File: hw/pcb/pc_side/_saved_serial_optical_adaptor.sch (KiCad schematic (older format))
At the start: 13 parts, among them P1 USB_B, P2 CONN_01X06, U1 LM393, U2 CP2102

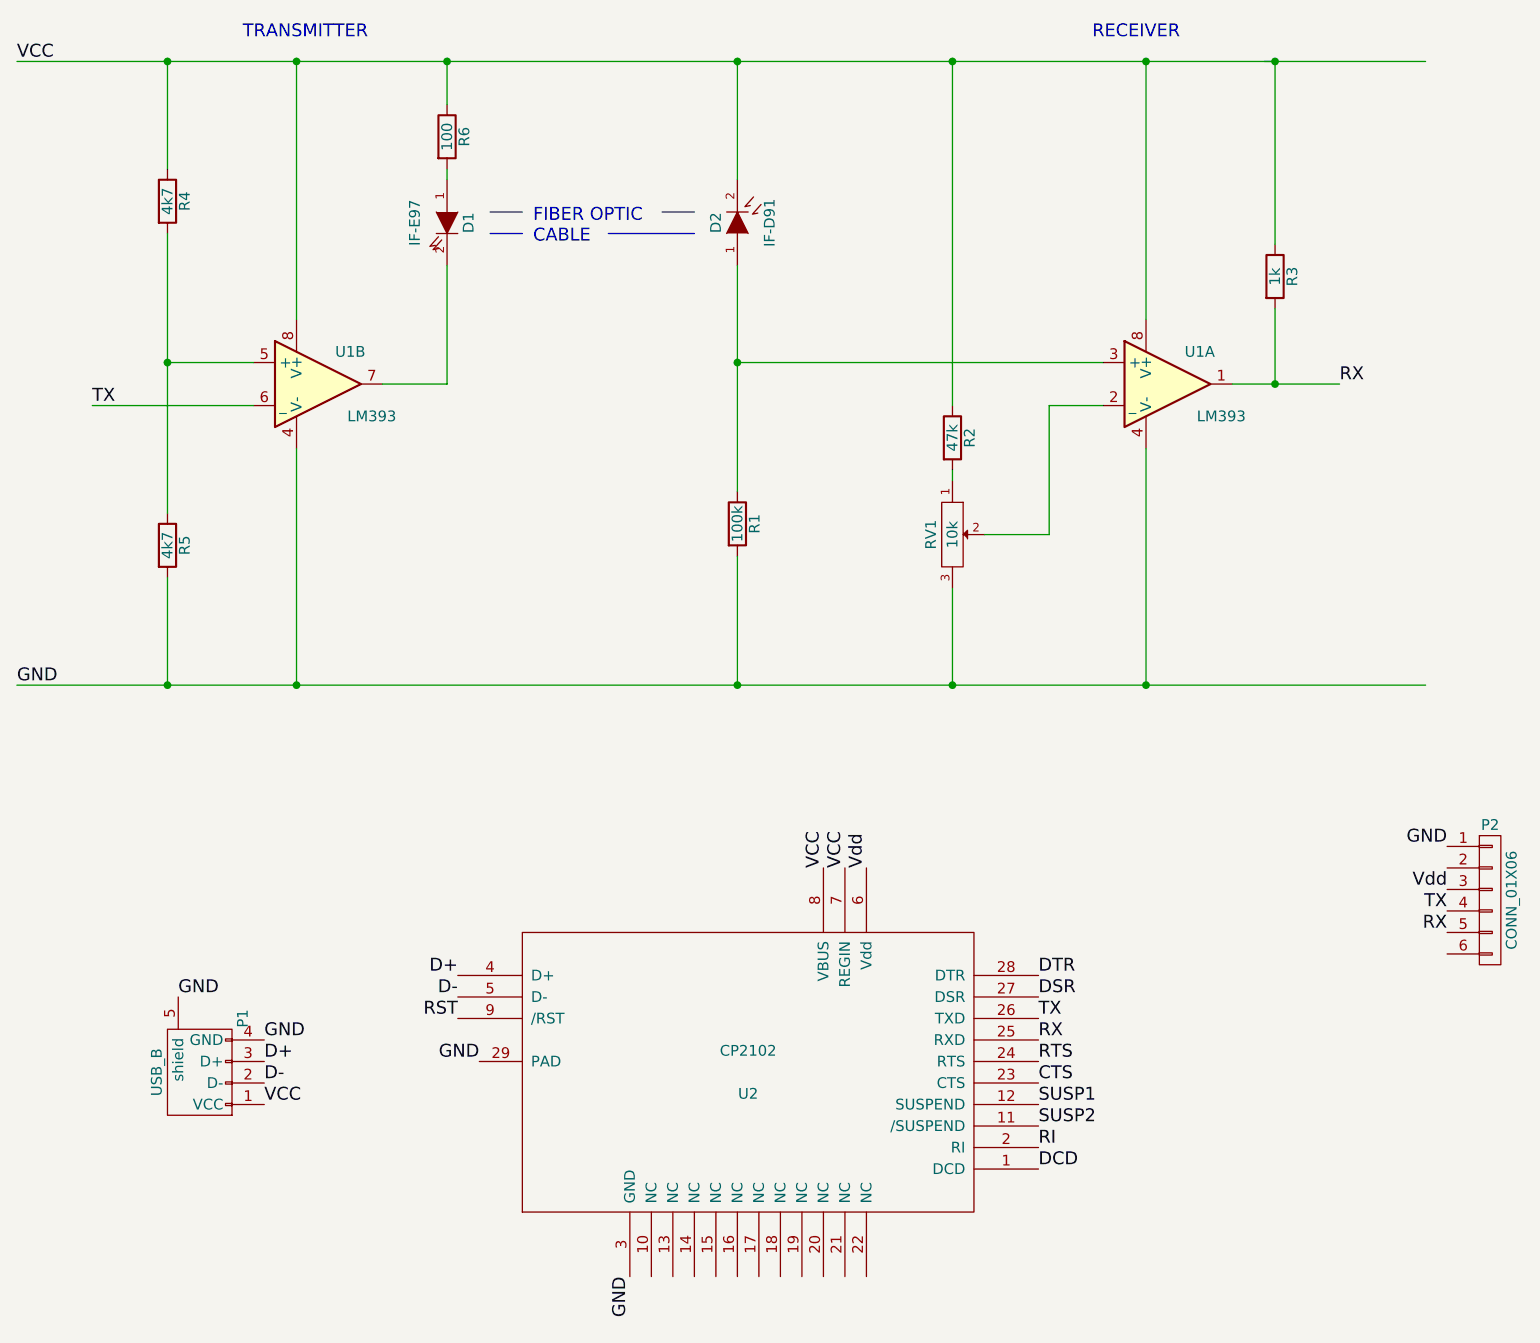
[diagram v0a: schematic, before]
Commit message: 
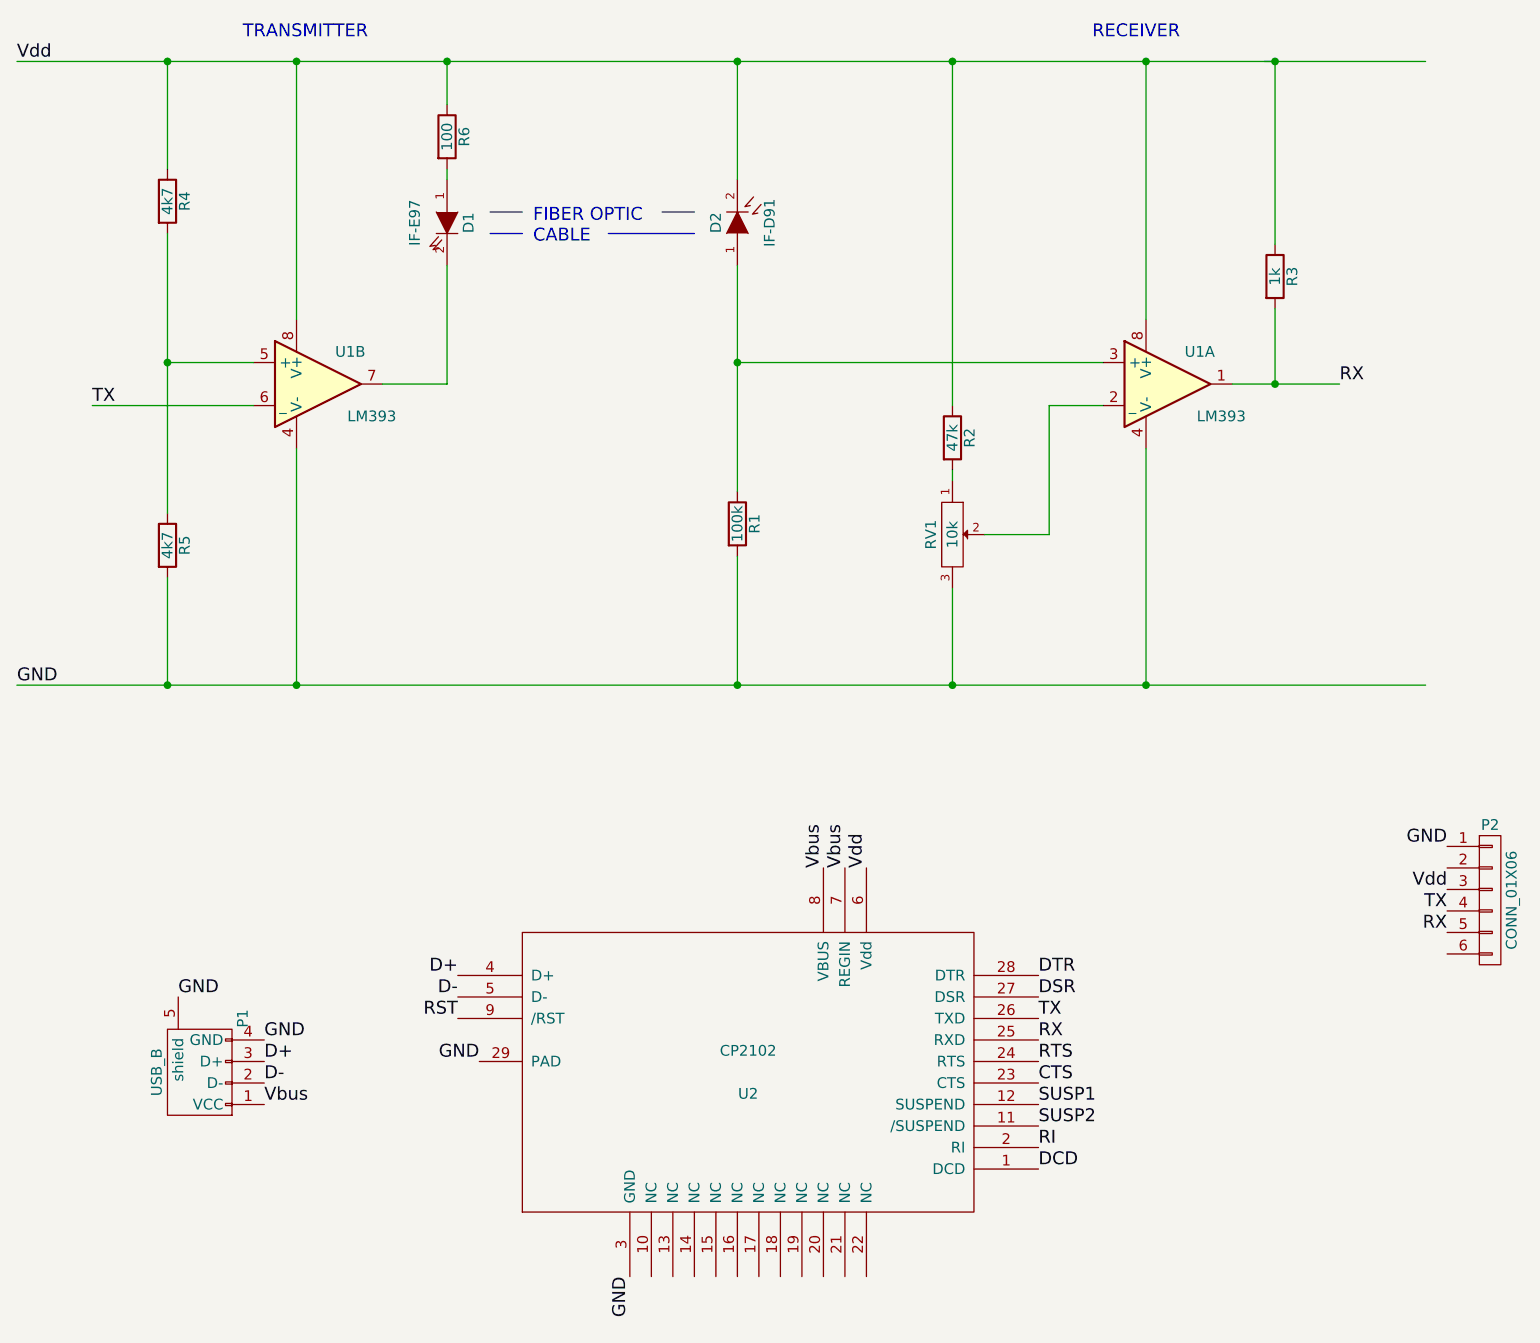
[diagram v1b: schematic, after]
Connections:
- net labels added: Vbus
- net labels removed: VCC
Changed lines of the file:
@@
 GND
 Text Label 650  750  0    60   ~ 0
-VCC
+Vdd
 Text Notes 5650 650  0    60   ~ 0
 RECEIVER
@@
 D-
 Text Label 1800 5600 0    60   ~ 0
-VCC
+Vbus
 Text Label 1800 5300 0    60   ~ 0
 GND
@@
 D-
 Text Label 4400 4500 1    60   ~ 0
-VCC
+Vbus
 Text Label 2700 5200 2    60   ~ 0
 RST
@@
 SUSP2
 Text Label 4500 4500 1    60   ~ 0
-VCC
+Vbus
 Text Label 5400 5000 0    60   ~ 0
 DTR
